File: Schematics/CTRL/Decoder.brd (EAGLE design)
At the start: 223.2 x 125.4 mm, 187 parts

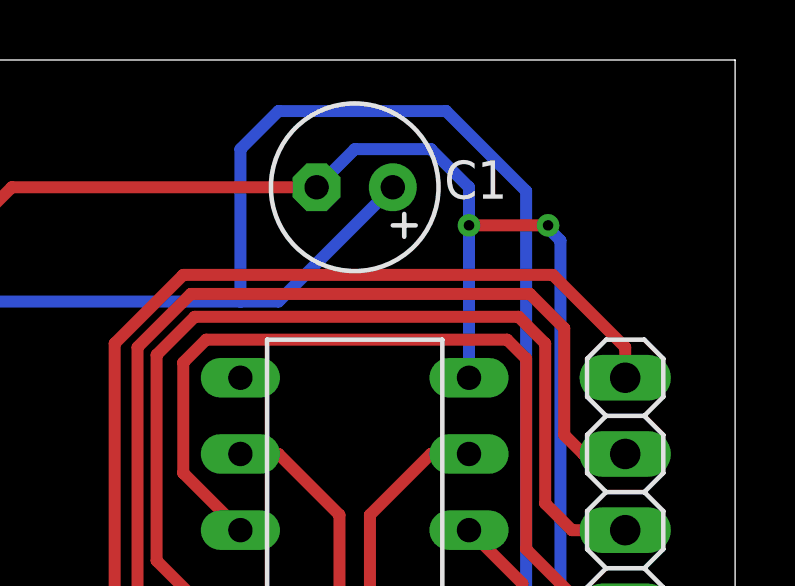
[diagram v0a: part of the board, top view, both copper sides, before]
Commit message: IR reg now have cp pin
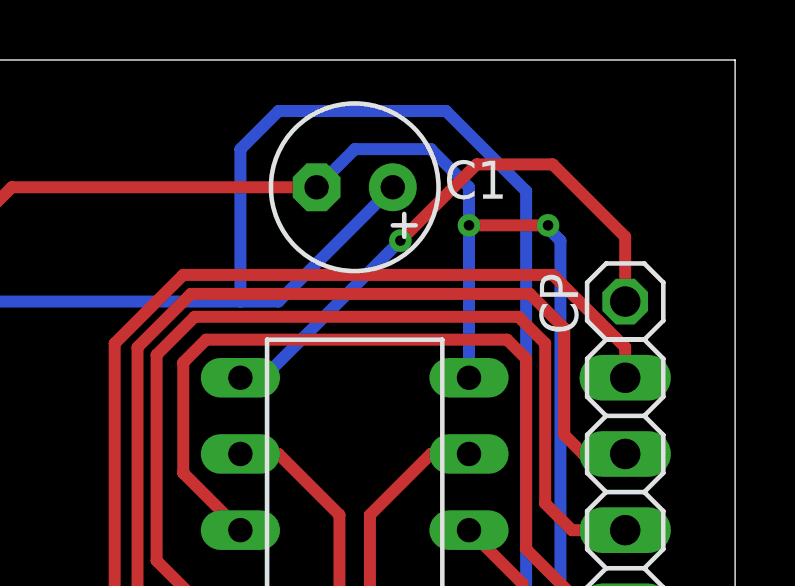
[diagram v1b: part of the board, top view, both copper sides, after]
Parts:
- added CP: (no value), pinhead:1X01
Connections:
- net IR-CP: now also CP.1
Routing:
- net IR-CP: track 0.00 -> 18.9 mm, vias 0 -> 1
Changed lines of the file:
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@@
 <attribute name="VALUE" x="81.153" y="33.655" size="1.27" layer="27" ratio="10" rot="R90"/>
+</element>
+<element name="CP" library="pinhead" library_urn="urn:adsk.eagle:library:325" package="1X01" package3d_urn="urn:adsk.eagle:package:22485/2" value="" x="219.583" y="117.348" smashed="yes">
+<attribute name="NAME" x="218.0082" y="116.2558" size="1.27" layer="25" ratio="10" rot="R90"/>
+<attribute name="POPULARITY" value="64" x="219.583" y="117.348" size="1.778" layer="27" display="off"/>
+<attribute name="VALUE" x="218.313" y="114.173" size="1.27" layer="27"/>
 </element>
 </elements>
@@
 <signal name="IR-CP">
 <contactref element="IR" pad="11"/>
+<contactref element="CP" pad="1"/>
+<wire x1="206.756" y1="114.808" x2="207.518" y2="114.808" width="0.4" layer="16"/>
+<wire x1="207.518" y1="114.808" x2="212.09" y2="119.38" width="0.4" layer="16"/>
+<via x="212.09" y="119.38" extent="1-16" drill="0.35"/>
+<wire x1="214.63" y1="121.92" x2="217.17" y2="121.92" width="0.4" layer="1"/>
+<wire x1="217.17" y1="121.92" x2="219.583" y2="119.507" width="0.4" layer="1"/>
+<wire x1="219.583" y1="119.507" x2="219.583" y2="117.348" width="0.4" layer="1"/>
+<wire x1="212.09" y1="119.38" x2="214.63" y2="121.92" width="0.4" layer="1"/>
 </signal>
 <signal name="N$10">
